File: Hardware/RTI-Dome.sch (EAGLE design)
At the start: 49 parts, among them IC1 24AA128ST, IC2 74LVC244, IC3 FT232RL, IC4 74ABT244, X13 PN61729-S

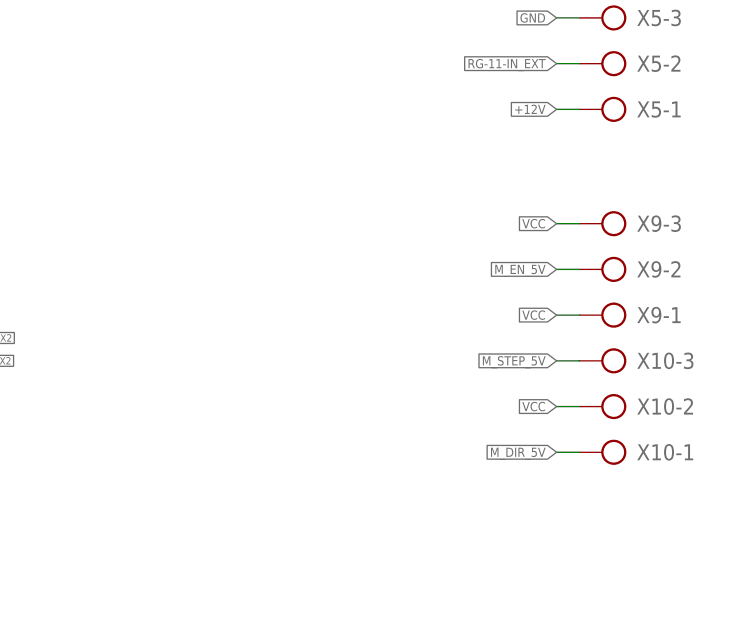
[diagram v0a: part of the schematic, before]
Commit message: fix the stepper connection to match the TB6600 and work with the ISD02/04/08 controller with the same settings
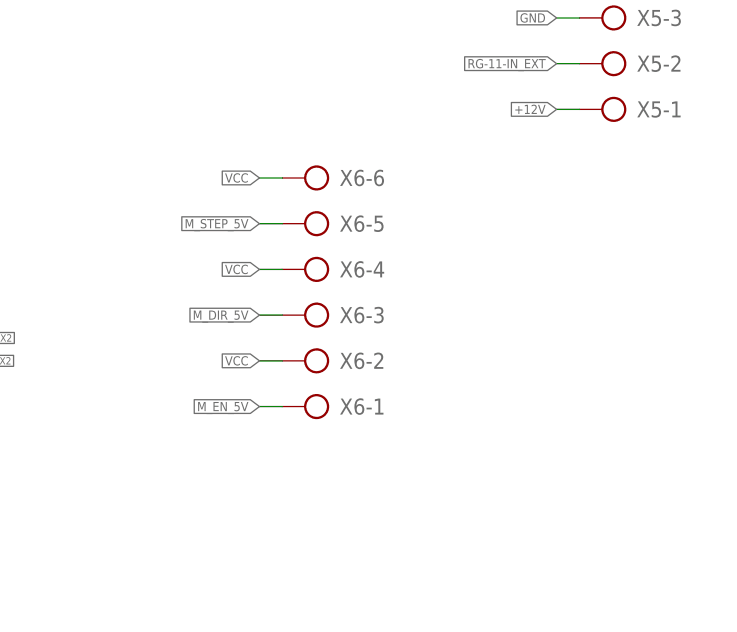
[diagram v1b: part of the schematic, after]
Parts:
- removed X10, X9: (no value), con-ptr500:AK500/3
- added X6: (no value), con-ptr500:AK500/6
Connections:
- net M_DIR_5V: now also X6-3.KL; no longer X10-1.KL
- net M_EN_5V: now also X6-1.KL; no longer X9-2.KL
- net M_STEP_5V: now also X6-5.KL; no longer X10-3.KL
- net VCC: now also X6-2.KL, X6-4.KL, X6-6.KL; no longer X10-2.KL, X9-1.KL, X9-3.KL
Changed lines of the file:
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@@
 <part name="GND3" library="supply1" deviceset="GND" device=""/>
 <part name="X8" library="con-ptr500" deviceset="AK500/2" device=""/>
-<part name="X9" library="con-ptr500" deviceset="AK500/3" device=""/>
-<part name="X10" library="con-ptr500" deviceset="AK500/3" device=""/>
 <part name="X11" library="con-ptr500" deviceset="AK500/2" device=""/>
 <part name="IC1" library="microchip" deviceset="24*" device="ST" technology="AA128"/>
@@
 <part name="R21" library="rti" deviceset="R-EU" device="'0805'" value="4.7K"/>
 <part name="FRAME1" library="frames" deviceset="DINA3_L" device=""/>
+<part name="X6" library="con-ptr500" deviceset="AK500/6" device=""/>
 </parts>
 <sheets>
@@
 <instance part="X8" gate="-1" x="378.46" y="111.76" rot="R180"/>
 <instance part="X8" gate="-2" x="378.46" y="116.84" rot="R180"/>
-<instance part="X9" gate="-1" x="378.46" y="175.26" rot="R180"/>
-<instance part="X9" gate="-2" x="378.46" y="180.34" rot="R180"/>
-<instance part="X9" gate="-3" x="378.46" y="185.42" rot="R180"/>
-<instance part="X10" gate="-1" x="378.46" y="160.02" rot="R180"/>
-<instance part="X10" gate="-2" x="378.46" y="165.1" rot="R180"/>
-<instance part="X10" gate="-3" x="378.46" y="170.18" rot="R180"/>
 <instance part="X11" gate="-1" x="378.46" y="99.06" rot="R180"/>
 <instance part="X11" gate="-2" x="378.46" y="104.14" rot="R180"/>
@@
 <instance part="FRAME1" gate="G$1" x="0" y="0"/>
 <instance part="FRAME1" gate="G$2" x="287.02" y="0"/>
+<instance part="X6" gate="-1" x="345.44" y="165.1" rot="R180"/>
+<instance part="X6" gate="-2" x="345.44" y="170.18" rot="R180"/>
+<instance part="X6" gate="-3" x="345.44" y="175.26" rot="R180"/>
+<instance part="X6" gate="-4" x="345.44" y="180.34" rot="R180"/>
+<instance part="X6" gate="-5" x="345.44" y="185.42" rot="R180"/>
+<instance part="X6" gate="-6" x="345.44" y="190.5" rot="R180"/>
 </instances>
 <busses>
@@
 </segment>
 <segment>
-<wire x1="370.84" y1="170.18" x2="373.38" y2="170.18" width="0.1524" layer="91"/>
-<label x="370.84" y="170.18" size="1.016" layer="95" rot="MR0" xref="yes"/>
-<pinref part="X10" gate="-3" pin="KL"/>
-</segment>
-<segment>
 <pinref part="IC4" gate="G$1" pin="1Y1"/>
 <wire x1="218.44" y1="246.38" x2="215.9" y2="246.38" width="0.1524" layer="91"/>
 <label x="218.44" y="246.38" size="1.016" layer="95" xref="yes"/>
 </segment>
+<segment>
+<wire x1="337.82" y1="185.42" x2="340.36" y2="185.42" width="0.1524" layer="91"/>
+<label x="337.82" y="185.42" size="1.016" layer="95" rot="MR0" xref="yes"/>
+<pinref part="X6" gate="-5" pin="KL"/>
+</segment>
 </net>
 <net name="M_DIR_5V" class="0">
@@
 </segment>
 <segment>
-<wire x1="370.84" y1="160.02" x2="373.38" y2="160.02" width="0.1524" layer="91"/>
-<label x="370.84" y="160.02" size="1.016" layer="95" rot="MR0" xref="yes"/>
-<pinref part="X10" gate="-1" pin="KL"/>
-</segment>
-<segment>
 <pinref part="IC4" gate="G$1" pin="2Y0"/>
 <wire x1="218.44" y1="251.46" x2="215.9" y2="251.46" width="0.1524" layer="91"/>
 <label x="218.44" y="251.46" size="1.016" layer="95" xref="yes"/>
 </segment>
+<segment>
+<wire x1="337.82" y1="175.26" x2="340.36" y2="175.26" width="0.1524" layer="91"/>
+<label x="337.82" y="175.26" size="1.016" layer="95" rot="MR0" xref="yes"/>
+<pinref part="X6" gate="-3" pin="KL"/>
+</segment>
 </net>
 <net name="M_EN_5V" class="0">
@@
 </segment>
 <segment>
-<wire x1="370.84" y1="180.34" x2="373.38" y2="180.34" width="0.1524" layer="91"/>
-<label x="370.84" y="180.34" size="1.016" layer="95" rot="MR0" xref="yes"/>
-<pinref part="X9" gate="-2" pin="KL"/>
-</segment>
-<segment>
 <pinref part="IC4" gate="G$1" pin="1Y0"/>
 <wire x1="218.44" y1="256.54" x2="215.9" y2="256.54" width="0.1524" layer="91"/>
 <label x="218.44" y="256.54" size="1.016" layer="95" xref="yes"/>
+</segment>
+<segment>
+<wire x1="337.82" y1="165.1" x2="340.36" y2="165.1" width="0.1524" layer="91"/>
+<label x="337.82" y="165.1" size="1.016" layer="95" rot="MR0" xref="yes"/>
+<pinref part="X6" gate="-1" pin="KL"/>
 </segment>
 </net>
@@
 </segment>
 <segment>
-<wire x1="370.84" y1="185.42" x2="373.38" y2="185.42" width="0.1524" layer="91"/>
-<label x="370.84" y="185.42" size="1.016" layer="95" rot="MR0" xref="yes"/>
-<pinref part="X9" gate="-3" pin="KL"/>
-</segment>
-<segment>
-<wire x1="370.84" y1="175.26" x2="373.38" y2="175.26" width="0.1524" layer="91"/>
-<label x="370.84" y="175.26" size="1.016" layer="95" rot="MR0" xref="yes"/>
-<pinref part="X9" gate="-1" pin="KL"/>
-</segment>
-<segment>
-<wire x1="370.84" y1="165.1" x2="373.38" y2="165.1" width="0.1524" layer="91"/>
-<label x="370.84" y="165.1" size="1.016" layer="95" rot="MR0" xref="yes"/>
-<pinref part="X10" gate="-2" pin="KL"/>
-</segment>
-</net>
+<wire x1="337.82" y1="190.5" x2="340.36" y2="190.5" width="0.1524" layer="91"/>
+<label x="337.82" y="190.5" size="1.016" layer="95" rot="MR0" xref="yes"/>
+<pinref part="X6" gate="-6" pin="KL"/>
+</segment>
+<segment>
+<wire x1="337.82" y1="180.34" x2="340.36" y2="180.34" width="0.1524" layer="91"/>
+<label x="337.82" y="180.34" size="1.016" layer="95" rot="MR0" xref="yes"/>
+<pinref part="X6" gate="-4" pin="KL"/>
+</segment>
+<segment>
+<wire x1="337.82" y1="170.18" x2="340.36" y2="170.18" width="0.1524" layer="91"/>
+<label x="337.82" y="170.18" size="1.016" layer="95" rot="MR0" xref="yes"/>
+<pinref part="X6" gate="-2" pin="KL"/>
+</segment>
+</net>

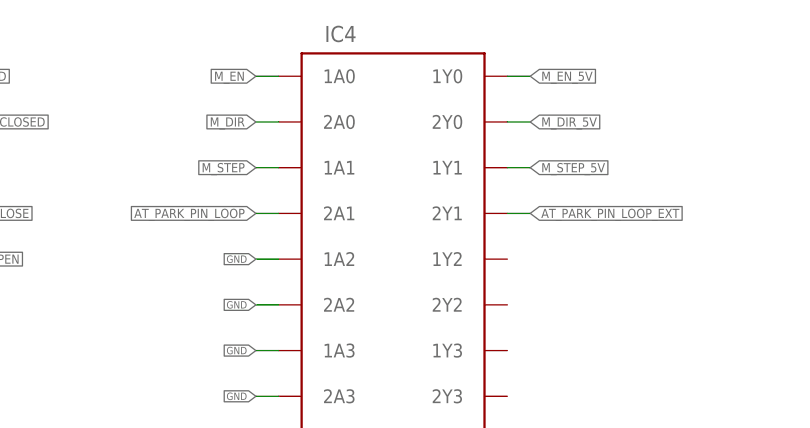
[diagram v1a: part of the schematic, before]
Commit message: rewire the 74ABT244 to help with routing
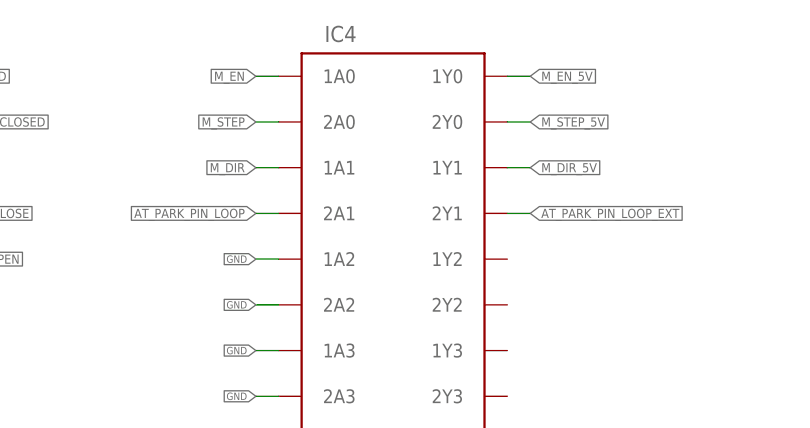
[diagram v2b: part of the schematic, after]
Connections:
- net M_DIR: now also IC4G$1.1A1; no longer IC4G$1.2A0
- net M_DIR_5V: now also IC4G$1.1Y1; no longer IC4G$1.2Y0
- net M_STEP: now also IC4G$1.2A0; no longer IC4G$1.1A1
- net M_STEP_5V: now also IC4G$1.2Y0; no longer IC4G$1.1Y1
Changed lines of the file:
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@@
+</segment>
+<segment>
+<pinref part="IC4" gate="G$1" pin="1A1"/>
+<wire x1="187.96" y1="246.38" x2="190.5" y2="246.38" width="0.1524" layer="91"/>
+<label x="187.96" y="246.38" size="1.016" layer="95" rot="R180" xref="yes"/>
+</segment>
+</net>
+<net name="M_STEP" class="0">
+<segment>
+<wire x1="83.82" y1="68.58" x2="81.28" y2="68.58" width="0.1524" layer="91"/>
+<label x="83.82" y="68.58" size="1.016" layer="95" xref="yes"/>
+<pinref part="PCB1" gate="G$1" pin="12"/>
 </segment>
 <segment>
@@
 <wire x1="187.96" y1="251.46" x2="190.5" y2="251.46" width="0.1524" layer="91"/>
 <label x="187.96" y="251.46" size="1.016" layer="95" rot="R180" xref="yes"/>
-</segment>
-</net>
-<net name="M_STEP" class="0">
-<segment>
-<wire x1="83.82" y1="68.58" x2="81.28" y2="68.58" width="0.1524" layer="91"/>
-<label x="83.82" y="68.58" size="1.016" layer="95" xref="yes"/>
-<pinref part="PCB1" gate="G$1" pin="12"/>
-</segment>
-<segment>
-<pinref part="IC4" gate="G$1" pin="1A1"/>
-<wire x1="187.96" y1="246.38" x2="190.5" y2="246.38" width="0.1524" layer="91"/>
-<label x="187.96" y="246.38" size="1.016" layer="95" rot="R180" xref="yes"/>
 </segment>
 </net>
@@
 </segment>
 <segment>
+<wire x1="337.82" y1="185.42" x2="340.36" y2="185.42" width="0.1524" layer="91"/>
+<label x="337.82" y="185.42" size="1.016" layer="95" rot="MR0" xref="yes"/>
+<pinref part="X6" gate="-5" pin="KL"/>
+</segment>
+<segment>
+<pinref part="IC4" gate="G$1" pin="2Y0"/>
+<wire x1="218.44" y1="251.46" x2="215.9" y2="251.46" width="0.1524" layer="91"/>
+<label x="218.44" y="251.46" size="1.016" layer="95" xref="yes"/>
+</segment>
+</net>
+<net name="M_DIR_5V" class="0">
+<segment>
+<label x="304.8" y="233.68" size="1.016" layer="95" rot="R270" xref="yes"/>
+<wire x1="304.8" y1="233.68" x2="304.8" y2="236.22" width="0.1524" layer="91"/>
+<pinref part="R19" gate="G$1" pin="2"/>
+</segment>
+<segment>
+<wire x1="337.82" y1="175.26" x2="340.36" y2="175.26" width="0.1524" layer="91"/>
+<label x="337.82" y="175.26" size="1.016" layer="95" rot="MR0" xref="yes"/>
+<pinref part="X6" gate="-3" pin="KL"/>
+</segment>
+<segment>
 <pinref part="IC4" gate="G$1" pin="1Y1"/>
 <wire x1="218.44" y1="246.38" x2="215.9" y2="246.38" width="0.1524" layer="91"/>
 <label x="218.44" y="246.38" size="1.016" layer="95" xref="yes"/>
 </segment>
-<segment>
-<wire x1="337.82" y1="185.42" x2="340.36" y2="185.42" width="0.1524" layer="91"/>
-<label x="337.82" y="185.42" size="1.016" layer="95" rot="MR0" xref="yes"/>
-<pinref part="X6" gate="-5" pin="KL"/>
-</segment>
-</net>
-<net name="M_DIR_5V" class="0">
-<segment>
-<label x="304.8" y="233.68" size="1.016" layer="95" rot="R270" xref="yes"/>
-<wire x1="304.8" y1="233.68" x2="304.8" y2="236.22" width="0.1524" layer="91"/>
-<pinref part="R19" gate="G$1" pin="2"/>
-</segment>
-<segment>
-<pinref part="IC4" gate="G$1" pin="2Y0"/>
-<wire x1="218.44" y1="251.46" x2="215.9" y2="251.46" width="0.1524" layer="91"/>
-<label x="218.44" y="251.46" size="1.016" layer="95" xref="yes"/>
-</segment>
-<segment>
-<wire x1="337.82" y1="175.26" x2="340.36" y2="175.26" width="0.1524" layer="91"/>
-<label x="337.82" y="175.26" size="1.016" layer="95" rot="MR0" xref="yes"/>
-<pinref part="X6" gate="-3" pin="KL"/>
-</segment>
-</net>
+</net>
